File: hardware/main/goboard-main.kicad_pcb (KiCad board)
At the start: 2 copper layers, 304.7 x 114.2 mm, 185 parts, among them J1 USB_C_Receptacle_USB2.0, J2 Conn_02x05_Top_Bottom, J3 Conn_01x01, Q1 SSM3J338R, Q2 BCP53, Q3 SSM3J338R, Q4 BC817, Q5 SSM3J338R, Q6 BC807, Q7 BC817, Q8 BC817, SW1 Esc, SW10 a, SW11 SW_Push, SW12 Fn, SW13 F2, SW14 2, SW15 w, SW16 s, SW17 z, SW18 Tux, SW19 F3, SW2 F1, SW20 3, SW21 e, SW22 d, SW23 c, SW24 Alt, SW25 F4, SW26 4, SW27 r, SW28 f, SW29 v, SW3 tilde, SW30 SW_DP3T, SW31 F5, SW32 5, SW33 t, SW34 g, SW35 b, SW36 F6, SW37 6, SW38 y, SW39 h, SW4 Tab, SW40 n, SW41 F7, SW42 7, SW43 u, SW44 j, SW45 m, SW46 Space, SW47 F8, SW48 8, SW49 i, SW5 Caps Lock, SW50 k, SW51 comma, SW52 F9, SW53 9, SW54 o, SW55 l, SW56 dot, SW57 F10, SW58 0, SW59 p, SW6 Shift, SW60 semicolon, SW61 slash, SW62 Alt Gr, SW63 F11, SW64 minus, SW65 sq br open, SW66 apostrophe, SW67 Menu, SW68 F12, SW69 equal, SW7 Ctrl, SW70 sq br close, SW71 backslash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

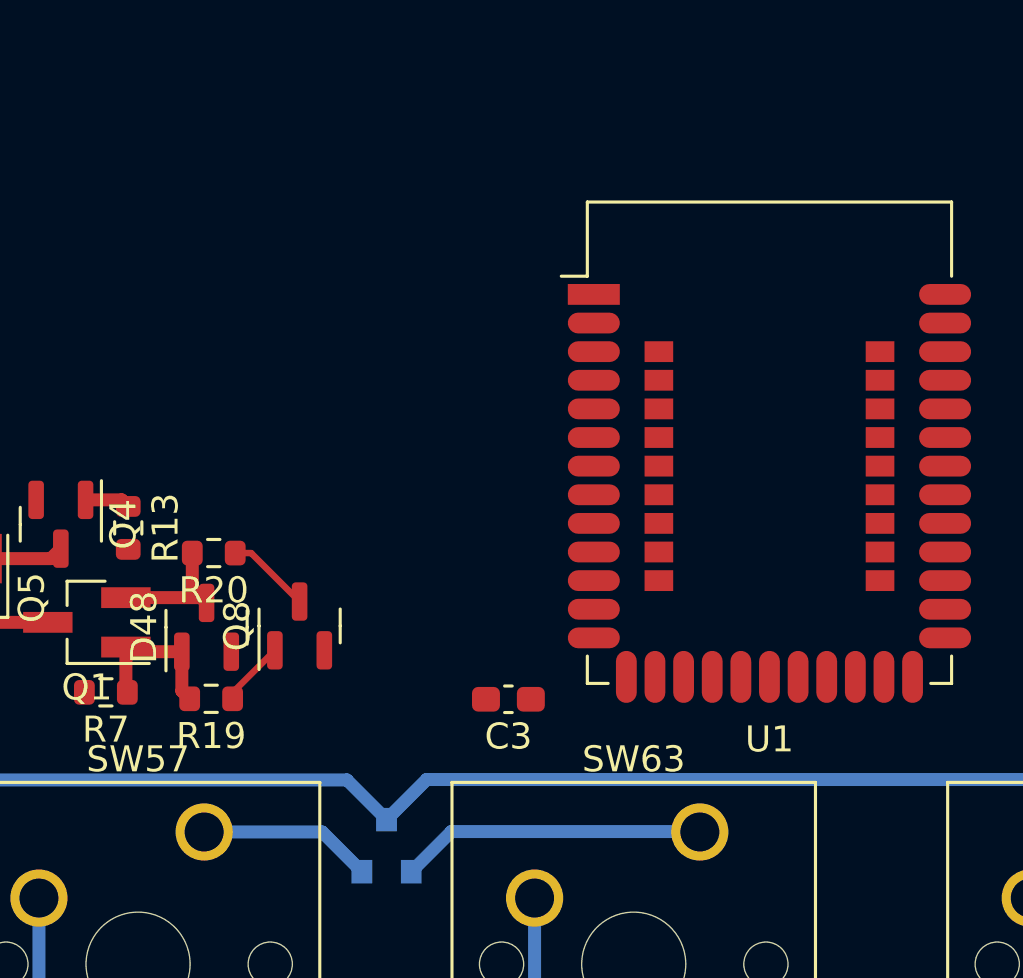
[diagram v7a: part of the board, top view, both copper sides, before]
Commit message: Add V_BUS connection for the MCU board
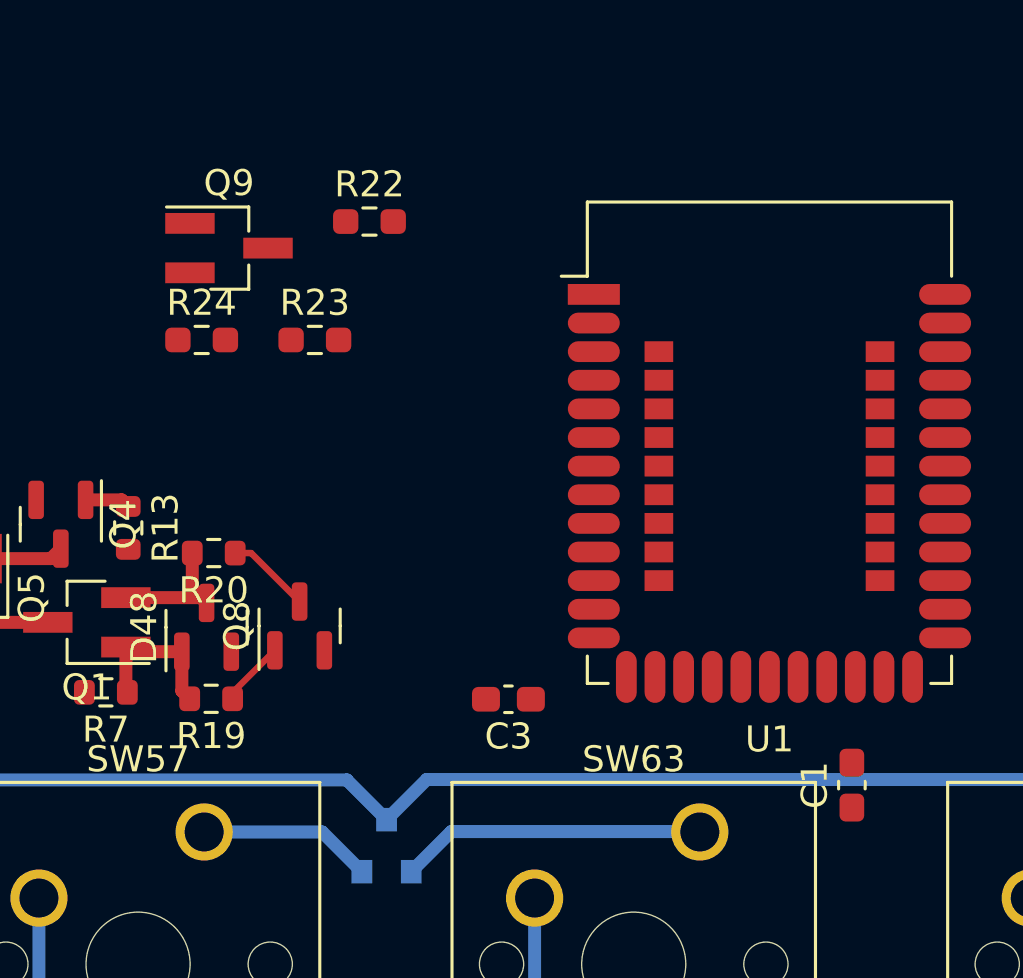
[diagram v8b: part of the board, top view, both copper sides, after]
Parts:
- added C1: 100nF, Capacitor_SMD:C_0603_1608Metric_Pad1.08x0.95mm_HandSolder, F.Cu at (265.4, 74.4)
- added Q9: SSM3J338R, Package_TO_SOT_SMD:SOT-23_Handsoldering, F.Cu at (241.5, 53.8)
- added R22: 100k, Resistor_SMD:R_0603_1608Metric_Pad0.98x0.95mm_HandSolder, F.Cu at (246.9, 52.7)
- added R23: 100k, Resistor_SMD:R_0603_1608Metric_Pad0.98x0.95mm_HandSolder, F.Cu at (244.8, 57.3)
- added R24: 100k, Resistor_SMD:R_0603_1608Metric_Pad0.98x0.95mm_HandSolder, F.Cu at (240.4, 57.3)
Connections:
- U1 pad 10: unconnected-(U1-Pad10) -> /MCU/MEAS_V_BATT
- U1 pad 11: unconnected-(U1-Pad11) -> /MCU/~ACT_MEAS_V_BATT
- U1 pad 22: (no net) -> +5V
